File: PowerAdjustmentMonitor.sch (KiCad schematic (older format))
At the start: 37 parts, among them U5 LM317K, U6 LM337T, U7 LM337T, U8 LM317

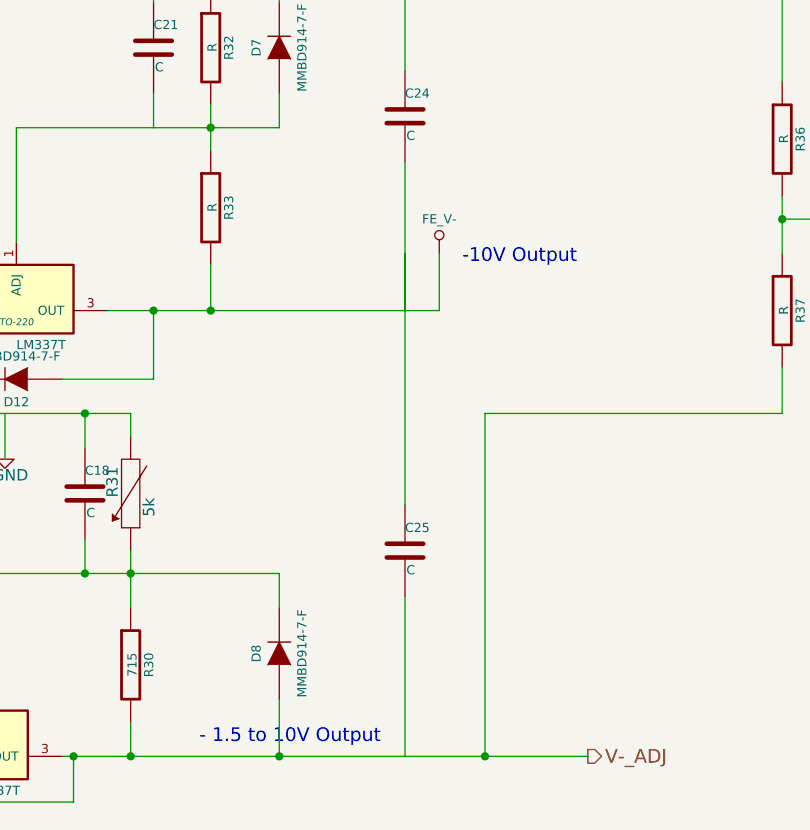
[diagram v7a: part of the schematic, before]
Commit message: 5.13 Video 2/2 Finalizing The System Part Placement
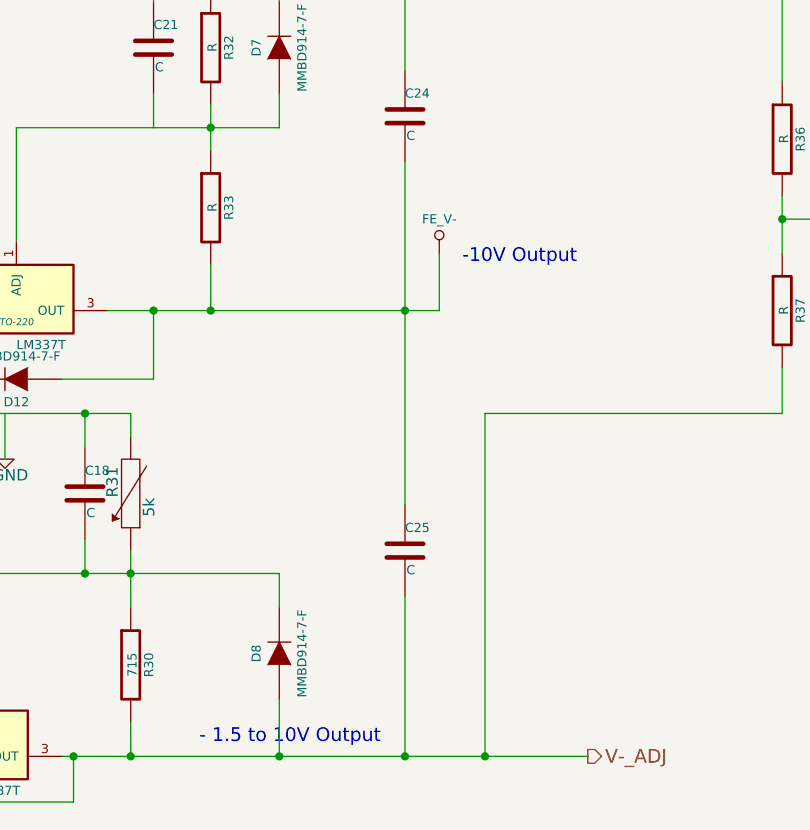
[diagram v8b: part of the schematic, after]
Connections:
- wire segments 101 -> 100
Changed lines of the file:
@@
 Connection ~ 5150 3900
 Wire Wire Line
-	5150 4950 5150 5600
-Wire Wire Line
-	5150 5350 5150 6450
+	5150 4950 5150 6450
 Wire Wire Line
 	5150 6850 5150 7550
@@
 	2000 7250 2500 7250
 Connection ~ 2500 7250
+Connection ~ 5150 5600
+Connection ~ 5150 7550
 $EndSCHEMATC
